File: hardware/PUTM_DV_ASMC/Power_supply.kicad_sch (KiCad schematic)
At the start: 0 parts

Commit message: schematics without main connector
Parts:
- added C13, C18, C20: 10u, Capacitor_SMD:C_0805_2012Metric_Pad1.18x1.45mm_HandSolder, symbol Device:C_Small
- added C14, C15, C22, C23: 100n, Capacitor_SMD:C_0603_1608Metric_Pad1.08x0.95mm_HandSolder, symbol Device:C_Small
- added C16, C19: 22u, Capacitor_SMD:CP_Elec_5x5.8, symbol Device:C_Polarized_Small
- added C17, C21, C24, C25, C26: 22u, Capacitor_SMD:C_0805_2012Metric_Pad1.18x1.45mm_HandSolder, symbol Device:C_Small
- added D5: 30V/200W, Diode_SMD:D_SOD-123, symbol Device:D_Zener_Small
- added D6: 9V1/200mW, Diode_SMD:D_SOD-323_HandSoldering, symbol Device:D_Zener_Small
- added D7: LED_+3V3, LED_SMD:LED_0603_1608Metric_Pad1.05x0.95mm_HandSolder, symbol Device:LED_Small
- added D8: LED_+5V, LED_SMD:LED_0603_1608Metric_Pad1.05x0.95mm_HandSolder, symbol Device:LED_Small
- added F1: 33V/1A5, Fuse:Fuse_2920_7451Metric_Pad2.10x5.45mm_HandSolder, symbol Device:Polyfuse_Small
- added F2, F3: 6V/1A, Fuse:Fuse_0805_2012Metric_Pad1.15x1.40mm_HandSolder, symbol Device:Polyfuse_Small
- added L1: 68u/1A4, Inductor_SMD:L_TDK_VLS6045EX_VLS6045AF, symbol Device:L_Small
- added Q1: 30V/5A, Package_TO_SOT_SMD:SOT-23-3, symbol Transistor_FET:Q_PMOS_GSD
- added R10, R14: 1k, Resistor_SMD:R_0603_1608Metric_Pad0.98x0.95mm_HandSolder, symbol Device:R_Small
- added R11: 510k, Resistor_SMD:R_0603_1608Metric_Pad0.98x0.95mm_HandSolder, symbol Device:R_Small
- added R12: 13k3, Resistor_SMD:R_0603_1608Metric_Pad0.98x0.95mm_HandSolder, symbol Device:R_Small
- added R13, R9: 100k, Resistor_SMD:R_0603_1608Metric_Pad0.98x0.95mm_HandSolder, symbol Device:R_Small
- added T1, T6: TP_VCC, TestPoint:TestPoint_Pad_1.0x1.0mm, symbol Connector:TestPoint_Small
- added T2, T8: TP_+5V, TestPoint:TestPoint_Pad_1.0x1.0mm, symbol Connector:TestPoint_Small
- added T3: TP_+3V3, TestPoint:TestPoint_Pad_1.0x1.0mm, symbol Connector:TestPoint_Small
- added T4, T5, T7, T9: TP_GND, TestPoint:TestPoint_Pad_1.0x1.0mm, symbol Connector:TestPoint_Small
- added U3: LM1117-3.3, Package_TO_SOT_SMD:SOT-223-3_TabPin2, symbol Regulator_Linear:LM1117MP-3.3
- added U4: TPS54202HDDCR, Package_TO_SOT_SMD:SOT-23-6_Handsoldering, symbol Regulator_Switching:TPS54202DDC
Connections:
- new net +24V: C16.1, C18.1, C19.1, C20.1, C21.1, C22.2, D6.1 (K), Q1.2 (S), R11.2, T6.1, U4.3 (VIN)
- new net +3V3: F2.2
- new net +5V: C13.1, C14.1, F3.1, T2.1, U3.3 (VI)
- new net +5V_OUT: C24.1, C25.1, C26.1, F3.2, L1.2, R13.2, R14.1, T8.1
- new net +BATT: F1.2
- new net BOOT_+5V: C23.1, U4.6 (BOOT)
- new net D3V3_R1k: D7.2 (A), R10.2
- new net D5V_R1k: D8.2 (A), R14.2
- new net EN: R11.1, U4.5 (EN)
- new net FB_+5V: R12.2, R13.1, U4.4 (FB)
- new net GND: C13.2, C14.2, C15.2, C16.2, C17.2, C18.2, C19.2, C20.2, C21.2, C22.1, C24.2, C25.2, C26.2, D5.2 (A), D7.1 (K), D8.1 (K), R12.1, R9.1, T4.1, T5.1, T7.1, T9.1, U3.1 (GND), U4.1 (GND)
- new net RPP_D: D5.1 (K), F1.1, Q1.3 (D), T1.1
- new net RPP_G: D6.2 (A), Q1.1 (G), R9.2
- new net SW_+5V: C23.2, L1.1, U4.2 (SW)
- new net VO_+3.3V: C15.1, C17.1, F2.1, R10.1, T3.1, U3.2 (VO)
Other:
- note added: "POWER +5V TO +3.3V"
- note added: "POWER VCC RPP & DECOUPLING"
- note added: "POWER VCC TO +5V"
- note added: "RPP"
- title: (none) -> Power Supply section

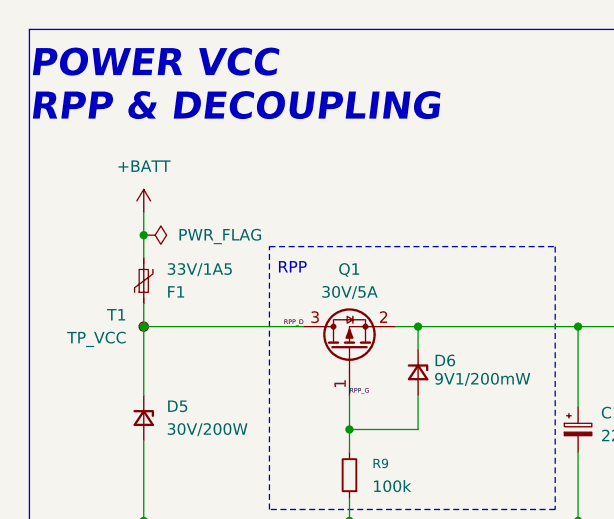
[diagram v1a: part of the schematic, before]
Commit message: tylko dwa bledy z can - schemat na wykonczeniu
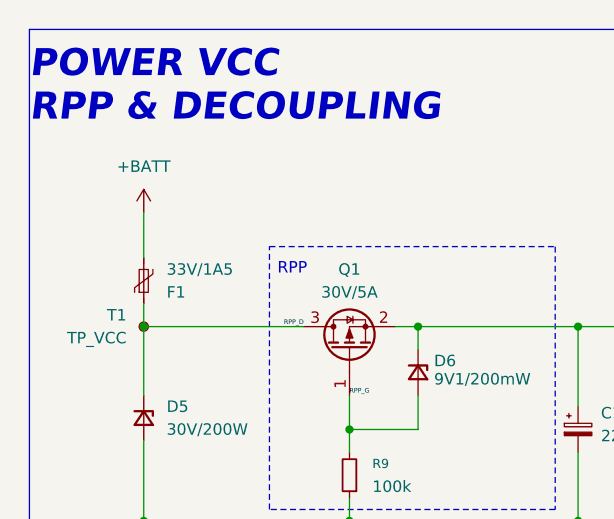
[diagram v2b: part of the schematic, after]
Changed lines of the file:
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@@
 	)
 	(junction
-		(at 39.37 57.15)
-		(diameter 0)
-		(color 0 0 0 0)
-	)
-	(junction
 		(at 59.69 137.16)
 		(diameter 0)
@@
 	(wire
 		(pts
-			(xy 39.37 54.61) (xy 39.37 57.15)
-		)
-		(stroke
-			(width 0)
-			(type default)
-		)
-	)
-	(wire
-		(pts
 			(xy 85.09 137.16) (xy 95.25 137.16)
 		)
@@
 	(wire
 		(pts
-			(xy 39.37 57.15) (xy 39.37 59.69)
+			(xy 39.37 54.61) (xy 39.37 59.69)
 		)
 		(stroke
@@
 					(unit 1)
 				)
-			)
-		)
-	)
-	(symbol
-		(lib_id "power:PWR_FLAG")
-		(at 39.37 57.15 270)
-		(unit 1)
-		(body_style 1)
-		(exclude_from_sim no)
-		(in_bom yes)
-		(on_board yes)
-		(in_pos_files yes)
-		(dnp no)
-		(fields_autoplaced yes)
-		(property "Reference" "#FLG01"
-			(at 41.275 57.15 0)
-			(hide yes)
-			(show_name no)
-			(do_not_autoplace no)
-			(effects
-				(font
-					(size 1.27 1.27)
-				)
-			)
-		)
-		(property "Value" "PWR_FLAG"
-			(at 43.18 57.1499 90)
-			(show_name no)
-			(do_not_autoplace no)
-			(effects
-				(font
-					(size 1.27 1.27)
-				)
-				(justify left)
-			)
-		)
-		(property "Footprint" ""
-			(at 39.37 57.15 0)
-			(hide yes)
-			(show_name no)
-			(do_not_autoplace no)
-			(effects
-				(font
-					(size 1.27 1.27)
-				)
-			)
-		)
-		(property "Datasheet" ""
-			(at 39.37 57.15 0)
-			(hide yes)
-			(show_name no)
-			(do_not_autoplace no)
-			(effects
-				(font
-					(size 1.27 1.27)
-				)
-			)
-		)
-		(property "Description" "Special symbol for telling ERC where power comes from"
-			(at 39.37 57.15 0)
-			(hide yes)
-			(show_name no)
-			(do_not_autoplace no)
-			(effects
-				(font
-					(size 1.27 1.27)
-				)
-			)
-		)
-		(pin "1"
-		)
-		(instances
-			(project "PUTM_DV_ASMC"
-				(path "/b652b05a-4e3d-4ad1-b032-18886abe7d45/76c3c659-a748-4932-81b3-d10dc40d628f"
-					(reference "#FLG01")
-					(unit 1)
-				)

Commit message: work work work
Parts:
- removed T4, T5, T7, T9: TP_GND, TestPoint:TestPoint_Pad_1.0x1.0mm, symbol Connector:TestPoint_Small
